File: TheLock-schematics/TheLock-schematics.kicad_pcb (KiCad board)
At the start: 2 copper layers, 12 parts, among them J1 CONN_SIGNAL, J2 CONN_POWER, J3 CONN_IRBOARD, J4 CONN_IRLED, Q1 PMV20XNE, Q2 IR PHOTOTRANS

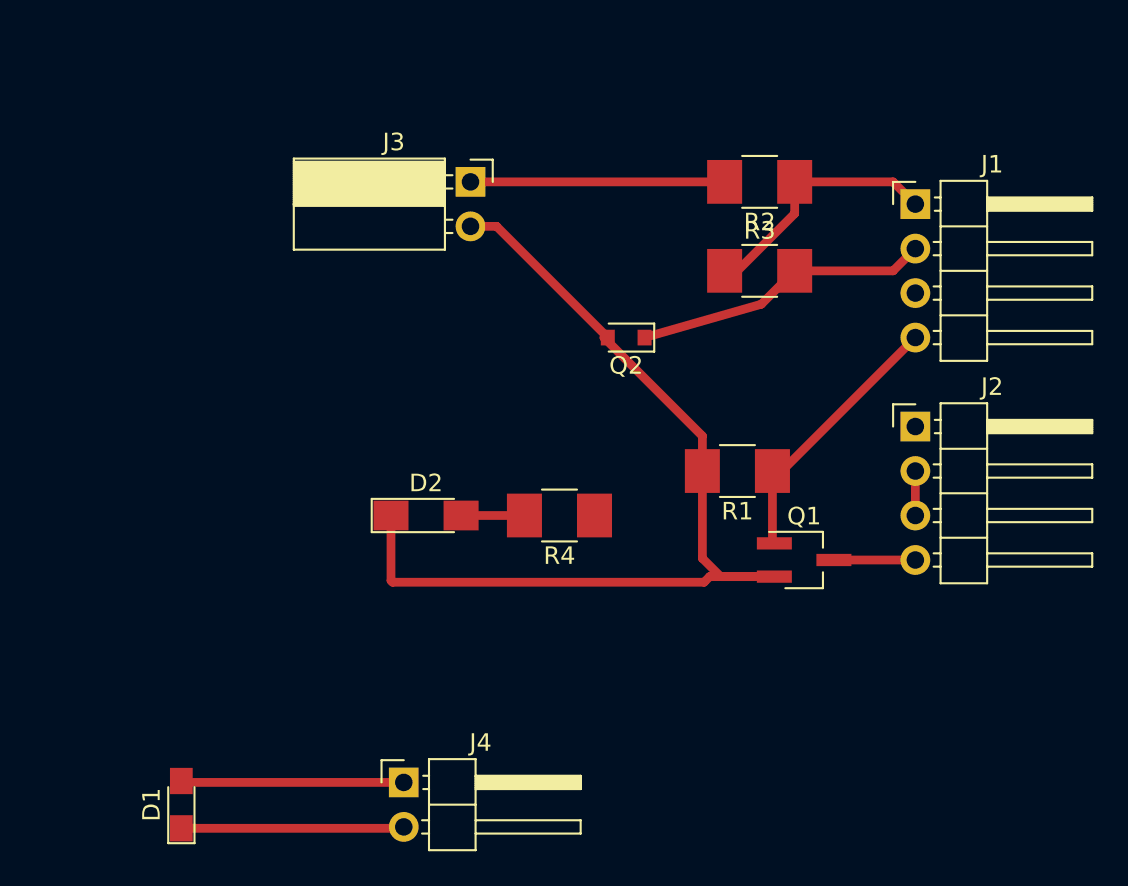
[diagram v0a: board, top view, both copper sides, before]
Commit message: electronics: PCB layout and mechanics should conform now
IR phototrans and LED should be positioned OK
PCB size and attachment should be roughly OK
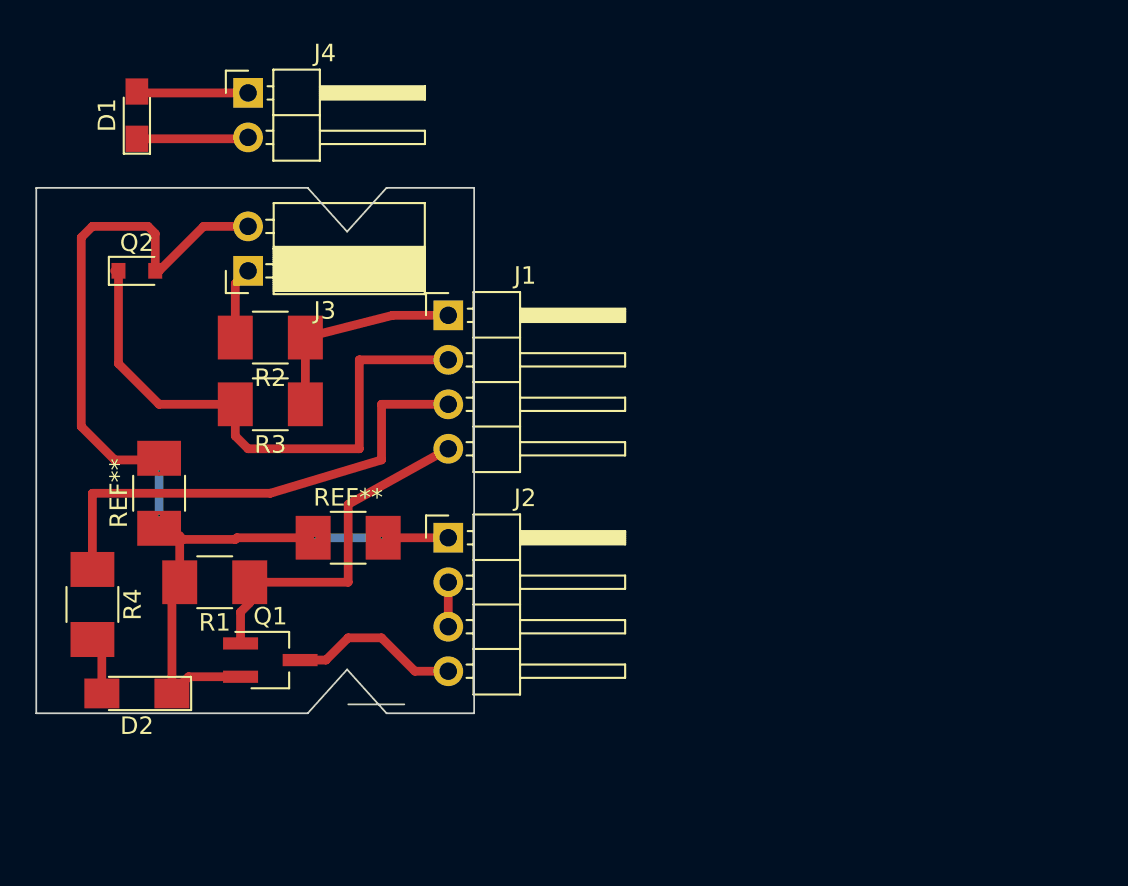
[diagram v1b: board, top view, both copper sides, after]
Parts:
- added REF**: R_1210_HandSoldering, Resistors_SMD:R_1210_HandSoldering, F.Cu at (109.9, 116.8)
- added REF**: R_1210_HandSoldering, Resistors_SMD:R_1210_HandSoldering, F.Cu at (99.1, 114.3)
- moved J4 40.4 mm to (104.1, 91.4)
- moved D1 39.5 mm to (97.8, 92.7)
- moved Q1 31.0 mm to (105.4, 123.8)
- moved R1 30.5 mm to (102.2, 119.4)
- moved R2 29.3 mm to (105.4, 105.4)
- moved R3 29.0 mm to (105.4, 109.2), turned to 180 degrees
- moved Q2 28.2 mm to (97.8, 101.6), turned to 0 degrees
- moved J2 27.4 mm to (115.6, 116.8)
- moved J1 27.4 mm to (115.6, 104.1)
- moved R4 27.1 mm to (95.2, 120.7), turned to 270 degrees
- moved D2 19.4 mm to (97.8, 125.7), turned to 180 degrees
- moved J3 13.7 mm to (104.1, 101.6), turned to 180 degrees
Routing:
- net status: track 0.00 -> 28.1 mm
- net keypresent: track 17.0 -> 32.5 mm
- net Net-(J3-Pad1): track 14.5 -> 4.11 mm
- net GNDPWR: track 55.9 -> 63.0 mm, vias 0 -> 4
- net Net-(D1-Pad2): track 12.7 -> 6.38 mm
- net Net-(D1-Pad1): track 12.7 -> 6.38 mm
- net unlock: track 15.6 -> 21.4 mm
- net solenoid-: track 4.65 -> 9.78 mm
- net +3V3: track 14.6 -> 12.1 mm
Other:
- board outline added: 25 x 30 mm

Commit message: electronics: Update to better accommodate LED
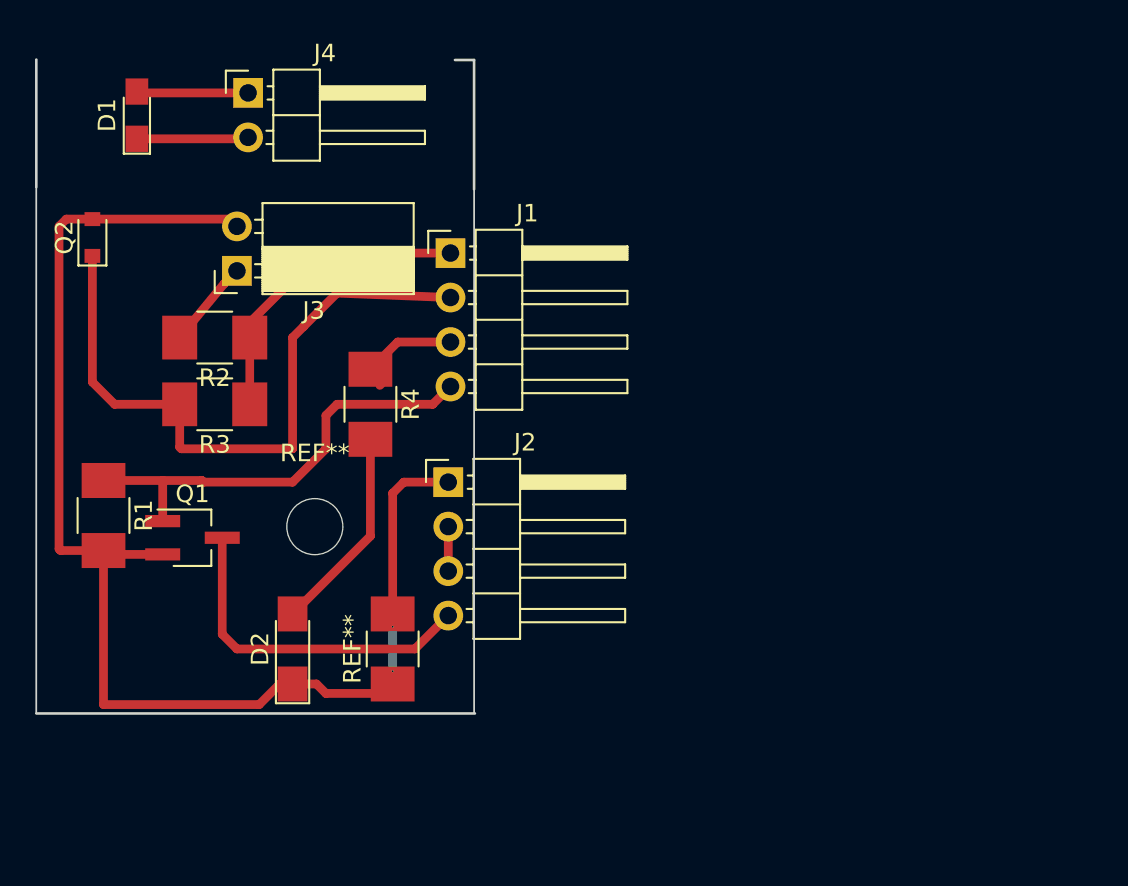
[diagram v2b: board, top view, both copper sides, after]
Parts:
- removed the REF** at (109.9, 116.8)
- removed the REF** at (99.1, 114.3)
- added REF**: R_1210_HandSoldering, Resistors_SMD:R_1210_HandSoldering, F.Cu at (112.4, 123.2)
- added REF**: MountingHole_3.2mm_M3, Mounting_Holes:MountingHole_3.2mm_M3, F.Cu at (108.0, 116.2)
- moved R4 19.6 mm to (111.1, 109.2)
- moved D2 9.25 mm to (106.7, 123.2), turned to 90 degrees
- moved Q1 8.28 mm to (101.0, 116.8)
- moved R1 7.41 mm to (95.9, 115.6), turned to 270 degrees
- moved J1 3.56 mm to (115.7, 100.6)
- moved Q2 3.18 mm to (95.2, 99.7), turned to 90 degrees
- moved J2 3.17 mm to (115.6, 113.7)
- moved R2 3.17 mm to (102.2, 105.4)
- moved R3 3.17 mm to (102.2, 109.2)
- moved J3 0.64 mm to (103.5, 101.6)
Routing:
- net status: track 28.1 -> 5.35 mm
- net GNDPWR: track 63.0 -> 76.1 mm, vias 4 -> 2
- net solenoid-: track 9.78 -> 19.6 mm
- net Net-(D2-Pad2): track 3.30 -> 11.8 mm
- net +3V3: track 12.1 -> 17.8 mm
- net keypresent: track 32.5 -> 38.1 mm
- net unlock: track 21.4 -> 25.7 mm
- net Net-(J3-Pad1): track 4.11 -> 5.02 mm
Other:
- board size 25 x 30 mm -> 25 x 37.3 mm
